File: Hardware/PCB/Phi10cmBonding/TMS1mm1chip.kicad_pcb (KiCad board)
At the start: 4 copper layers, 1 part, among them U1 TMS1mm

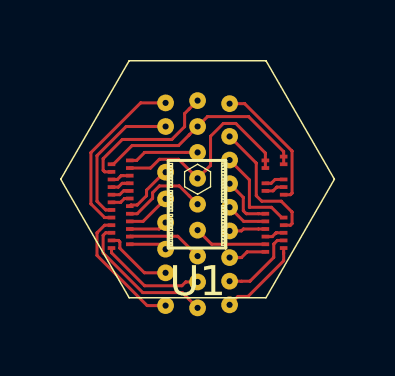
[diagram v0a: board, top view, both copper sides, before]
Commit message: Achieve reasonable array generation.
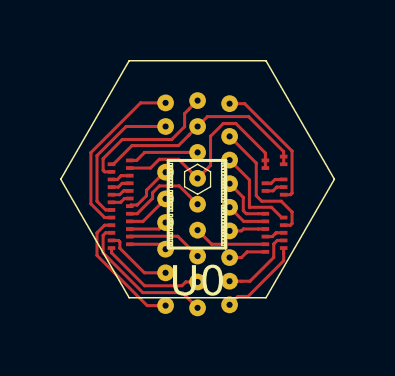
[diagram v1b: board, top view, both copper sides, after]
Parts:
- renumbered U1 to U0
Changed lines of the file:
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@@
   (module Topmetal:TMS1mm (layer F.Cu)
     (at 139.7 107.95)
-    (fp_text reference U1 (at 0 3.4) (layer F.SilkS)
+    (fp_text reference U0 (at 0 3.4) (layer F.SilkS)
       (effects (font (size 1 1) (thickness 0.15)))
     )
